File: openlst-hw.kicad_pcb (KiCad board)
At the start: 4 copper layers, 60 x 50 mm, 175 parts, among them J1 5VDC, J2 CC Prog/Debug, J3 UART0, J4 UART1, J5 Control Outputs, J6 ANT, U1 LM1117-3.3, U2 CC1110, U3 LT1086-3.6, U4 FOX924 27MHz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

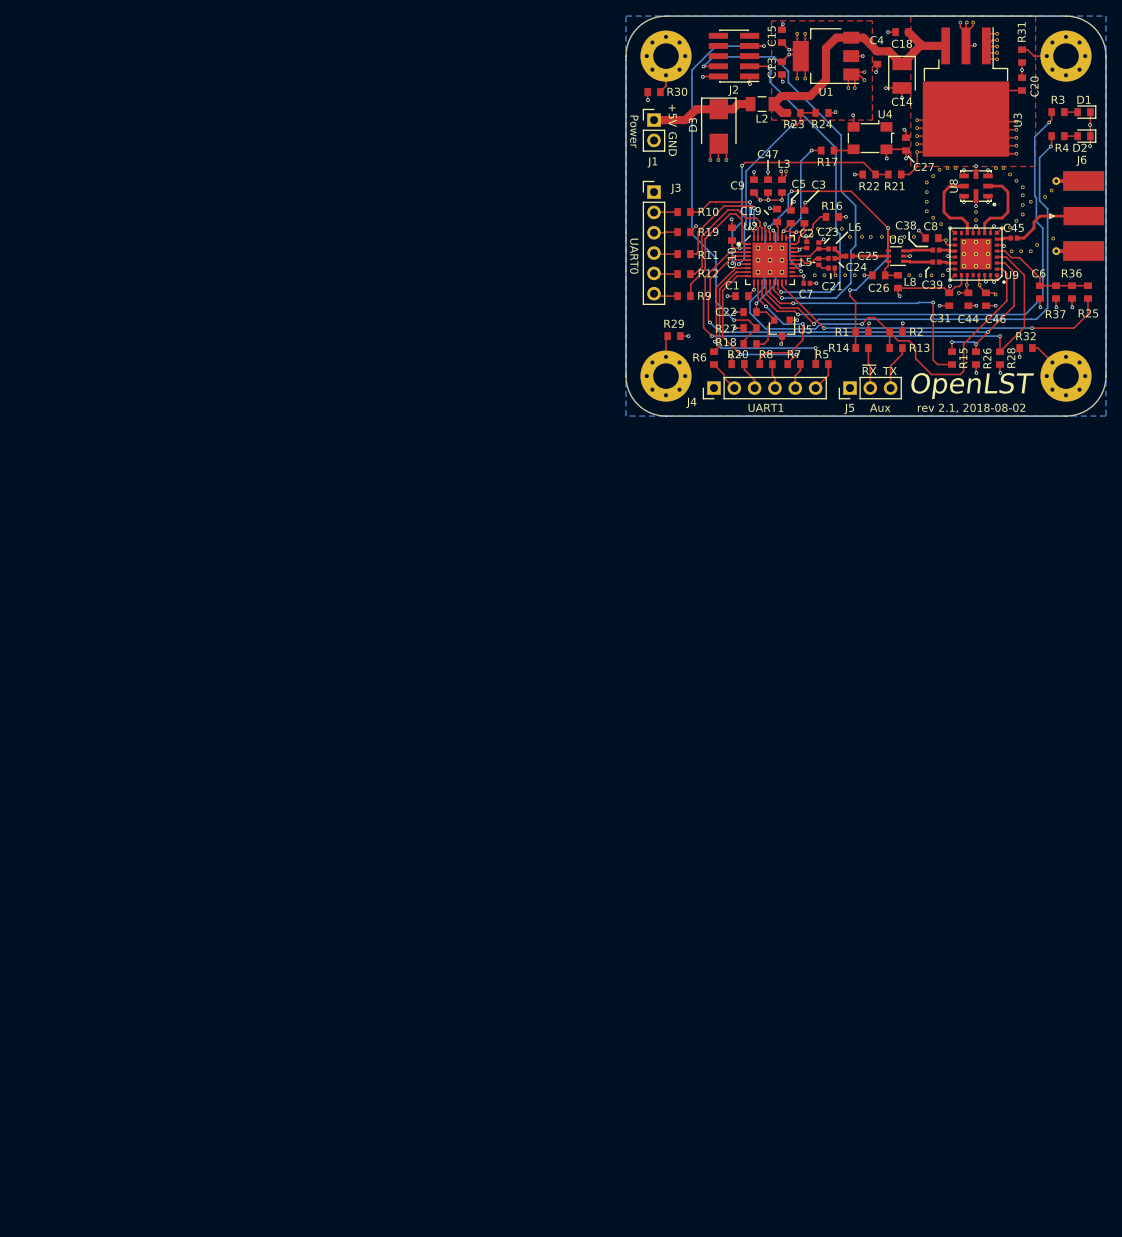
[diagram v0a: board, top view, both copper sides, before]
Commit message: CAM: commiting v2.2 (inprogress) which makes the openlst board fit in a PC104 stack and swaps an ldo
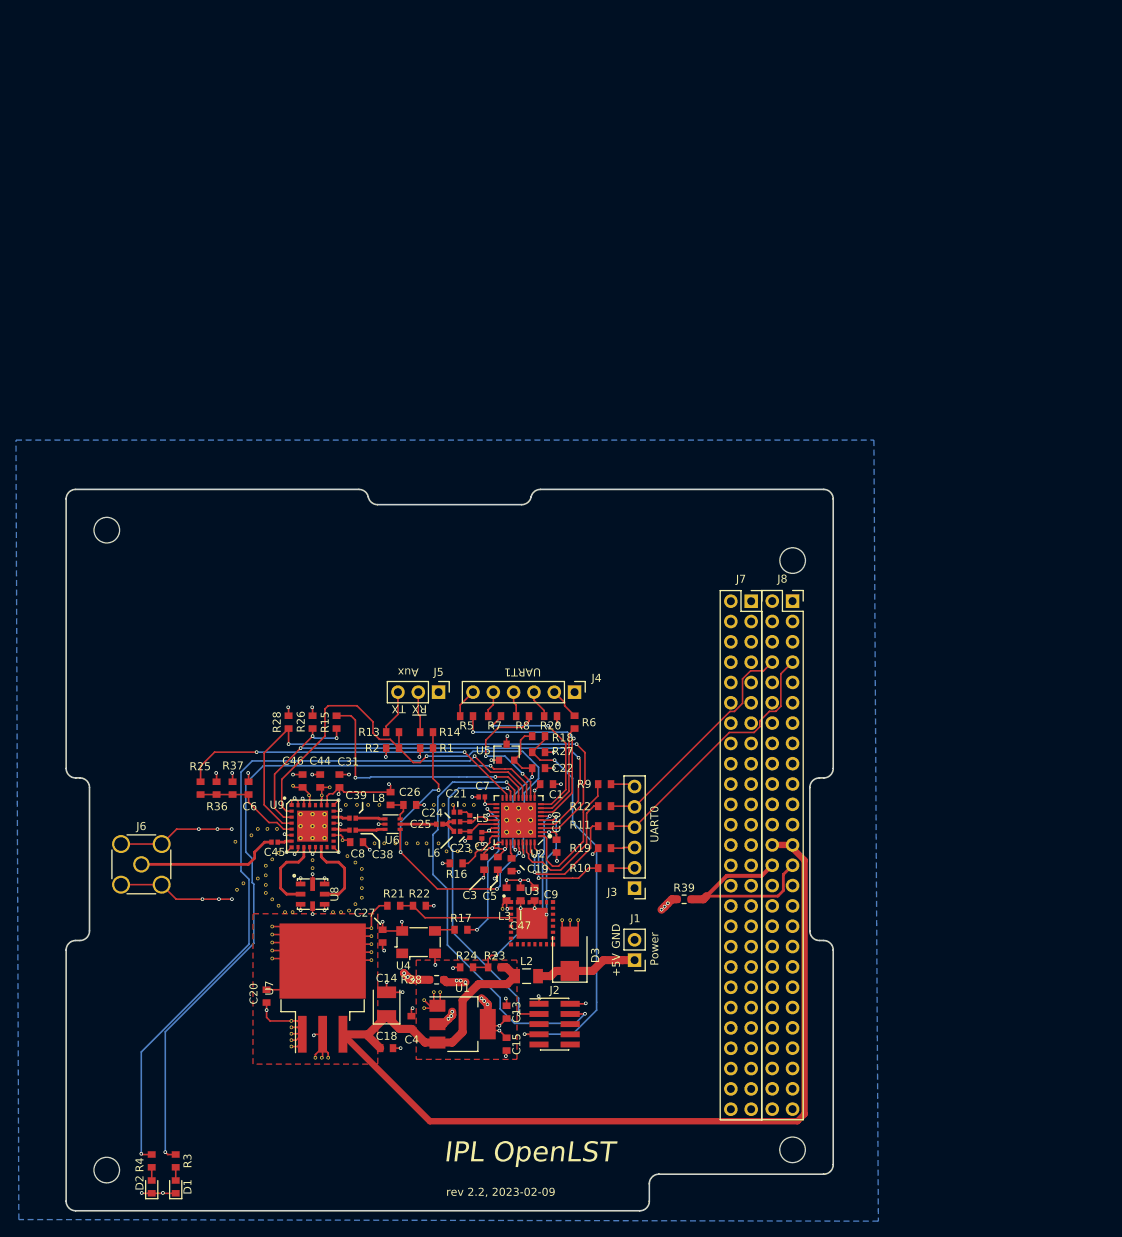
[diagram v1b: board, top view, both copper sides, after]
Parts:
- removed MK1, MK2, MK3, MK4: M3_Hole, archive:MountingHole_3.2mm_M3_Pad_Via
- removed R29, R30, R31, R32: DNI, archive:R_0603_1608Metric
- removed the REF** at (134.9, 46.3)
- removed the REF** at (135.9, 46.3)
- removed the REF** at (134.9, 40.7)
- removed the REF** at (135.9, 40.7)
- added J7: PC104-1, custom_connectors:PinSocket_2x26_P2.54mm_Vertical, F.Cu at (129.1, 111.6)
- added J8: PC104-2, custom_connectors:PinSocket_2x26_P2.54mm_Vertical, F.Cu at (134.3, 111.6)
- added R38: DNI, resistor_smd:R_0603_1608Metric_Pad0.98x0.95mm_HandSolder, F.Cu at (89.8, 159.0)
- added R39: DNI, resistor_smd:R_0603_1608Metric_Pad0.98x0.95mm_HandSolder, F.Cu at (120.8, 148.9)
- added REF1: MountingHole_3.2mm_M3, MountingHole:MountingHole_3.2mm_M3, F.Cu at (48.6, 102.8)
- added REF2: MountingHole_3.2mm_M3, MountingHole:MountingHole_3.2mm_M3, F.Cu at (134.3, 106.6)
- added REF3: MountingHole_3.2mm_M3, MountingHole:MountingHole_3.2mm_M3, F.Cu at (134.3, 180.2)
- added REF4: MountingHole_3.2mm_M3, MountingHole:MountingHole_3.2mm_M3, F.Cu at (48.6, 182.7)
- added U7: LT1685CM-3.6, TO_SOT_SMD:TO-263-3_TabPin2, F.Cu at (75.6, 160.0)
- C20: value 10u -> 22u
- J6: footprint archive:SMA_Molex_73251-1153_EdgeMount_Horizontal -> coax:SMA_Amphenol_132134_Vertical
- U3: value LT1086-3.6 -> RFFM6406; footprint archive:TO-263-3_TabPin2 -> openlst:Qorvo_LGA_28
- moved D1 175.9 mm to (57.2, 184.9), turned to 90 degrees
- moved D2 175.6 mm to (54.2, 184.9), turned to 90 degrees
- moved R3 171.3 mm to (57.2, 181.6), turned to 90 degrees
- moved R4 171.0 mm to (54.2, 181.6), turned to 90 degrees
- moved REF** 154.3 mm to (71.7, 167.3), turned to 180 degrees
- moved REF** 153.3 mm to (74.7, 168.7), turned to 180 degrees
- moved REF** 153.0 mm to (71.7, 166.5), turned to 180 degrees
- moved REF** 152.5 mm to (75.5, 168.7), turned to 180 degrees
- moved REF** 151.7 mm to (71.7, 165.7), turned to 180 degrees
- moved REF** 151.6 mm to (76.3, 168.7), turned to 180 degrees
- moved REF** 150.4 mm to (71.7, 164.9), turned to 180 degrees
- moved REF** 149.1 mm to (71.7, 164.1), turned to 180 degrees
- moved C20 148.0 mm to (68.6, 161.0), turned to -90 degrees
- moved C18 142.4 mm to (83.6, 167.5), turned to 0 degrees
- moved J6 141.6 mm to (52.9, 144.5), turned to 0 degrees
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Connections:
- net /~LST_RESET renamed /~{LST_RESET}
- net /~LST_RX_MODE renamed /~{LST_RX_MODE}
- C13 pad 1: +3V3 -> Net-(C13-Pad1)
- C15 pad 1: +3V3 -> Net-(C13-Pad1)
- D3 pad 1: Net-(D3-Pad1) -> 5V_VIN
- J2 pad 10: Net-(J2-Pad10) -> unconnected-(J2-Pad10)
- J2 pad 5: Net-(J2-Pad5) -> unconnected-(J2-Pad5)
- J2 pad 6: Net-(J2-Pad6) -> unconnected-(J2-Pad6)
- J2 pad 8: Net-(J2-Pad8) -> unconnected-(J2-Pad8)
- J2 pad 9: Net-(J2-Pad9) -> unconnected-(J2-Pad9)
- L2 pad 2: Net-(D3-Pad1) -> 5V_VIN
- U1 pad 2: +3V3 -> Net-(C13-Pad1)
- U2 pad 18: Net-(U2-Pad18) -> unconnected-(U2-Pad18)
- U2 pad 20: Net-(U2-Pad20) -> unconnected-(U2-Pad20)
- U3 pad 2: VCC_3V6 -> /LST_TX_MODE
- U3 pad 3: +5V -> /RF_EN
- U8 pad 2: Net-(U8-Pad2) -> Net-(U3-Pad10)
- U8 pad 6: Net-(U8-Pad6) -> Net-(U3-Pad13)
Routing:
- net +5V: track 34.7 -> 133.8 mm
- net GND: track 94.4 -> 150.9 mm, vias 56 -> 61
- net /AN0: track 33.9 -> 0.00 mm, vias 2 -> 0
- net Net-(R4-Pad2): track 61.6 -> 94.1 mm
- net /UART0_RX: track 3.00 -> 34.1 mm
- net Net-(R3-Pad2): track 63.1 -> 91.2 mm
- net Net-(C13-Pad1): track 0.00 -> 28.1 mm, vias 0 -> 11
- net /UART0_TX: track 2.99 -> 29.5 mm
- net Net-(J8-Pad27): track 0.00 -> 25.4 mm
- net +3V3: track 46.5 -> 33.2 mm, vias 15 -> 18
- net 5V_VIN: track 0.00 -> 12.9 mm
- net Net-(D3-Pad1): track 12.9 -> 0.00 mm
- net Net-(C45-Pad1): track 9.91 -> 17.9 mm
- net Net-(MK3-Pad1): track 5.83 -> 0.00 mm
- net Net-(MK4-Pad1): track 5.65 -> 0.00 mm
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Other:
- board size 60 x 50 mm -> 95.9 x 90.2 mm
- net class 50ohm removed
- net class 8mil removed
- net class Default removed
- net class PWR removed
- board text added: "IPL OpenLST"
- board text added: "rev 2.2, 2023-02-09"
- board text added: "~{RX}"
- board text removed: "OpenLST"
- board text removed: "rev 2.1, 2018-08-02"
- board text removed: "~RX"

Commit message: CAM: commiting current revision
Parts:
- removed J1: 5VDC, archive:PinHeader_1x02_P2.54mm_Vertical
- removed U9: RFFM6406, openlst:Qorvo_LGA_28_ThermalVias
- moved U3 30.0 mm to (74.3, 139.8)
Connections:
- J8 pad 25: +5V -> 5V_VIN
- J8 pad 26: +5V -> 5V_VIN
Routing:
- net +5V: track 133.8 -> 34.7 mm
- net 5V_VIN: track 12.9 -> 49.3 mm
- net /AN0: track 0.00 -> 33.9 mm, vias 0 -> 2
- net GND: track 150.9 -> 117.0 mm, vias 61 -> 59
- net Net-(U8-Pad6): track 10.0 -> 0.00 mm
- net Net-(U3-Pad13): track 0.00 -> 10.0 mm
- net Net-(U8-Pad2): track 10.0 -> 0.00 mm
- net Net-(U3-Pad10): track 0.00 -> 10.0 mm
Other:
- board text removed: "+5V"
- board text removed: "GND"
- board text removed: "Power"
